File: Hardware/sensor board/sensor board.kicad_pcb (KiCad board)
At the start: 2 copper layers, 10 parts, among them J1 Raspberry_Pi_2_3, J2 Bar30, J3 LPS331AP, J4 Conn_01x04_Pin, J5 Conn_01x04_Pin, U1 MTi_3

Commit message: updated 3d models
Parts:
- J1: footprint Connector_PinHeader_2.54mm:PinHeader_2x20_P2.54mm_Vertical -> Connector_PinSocket_2.54mm:PinSocket_2x20_P2.54mm_Vertical
- J4, J5: footprint Connector_JST:JST_XH_B4B-XH-AM_1x04_P2.50mm_Vertical -> Connector_JST:JST_XH_B4B-XH-A_1x04_P2.50mm_Vertical

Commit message: layout for sensor board
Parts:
- moved R1 94.7 mm to (52.5, 58.8)
- moved R2 94.7 mm to (52.5, 61.8)
- moved FB1 92.5 mm to (63.5, 48.0), turned to -90 degrees
- moved C1 91.6 mm to (63.5, 53.1), turned to 90 degrees
- moved U1 89.9 mm to (50.5, 49.3), turned to 180 degrees
- moved J5 87.5 mm to (45.1, 66.6), turned to 90 degrees
- moved J2 69.8 mm to (32.3, 50.2), turned to -90 degrees
- moved J4 67.7 mm to (31.9, 66.7), turned to 90 degrees
- moved J3 67.1 mm to (30.8, 22.1)
- moved J1 65.9 mm to (22.1, 67.8)
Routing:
- net GND: track 0.00 -> 119.2 mm
- net +3.3V: track 0.00 -> 111.7 mm, vias 0 -> 1
- net /SCL: track 0.00 -> 75.9 mm, vias 0 -> 1
- net /SDA: track 0.00 -> 66.8 mm, vias 0 -> 1
- net Net-(U1-VDDA): track 0.00 -> 8.72 mm

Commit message: Update sensor board.kicad_pcb
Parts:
- moved J5 20.8 mm to (65.9, 66.6)
- moved R1 20.8 mm to (73.3, 58.8)
- moved R2 20.8 mm to (73.3, 61.8)
- moved U1 20.8 mm to (71.3, 49.3)
- moved FB1 20.1 mm to (80.9, 58.1)
- moved C1 14.9 mm to (77.6, 58.0), turned to -90 degrees
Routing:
- net +3.3V: track 111.7 -> 117.5 mm
- net Net-(U1-VDDA): track 8.72 -> 13.8 mm
- net GND: track 119.2 -> 115.8 mm
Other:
- board outline added: 65.5 x 55.9 mm

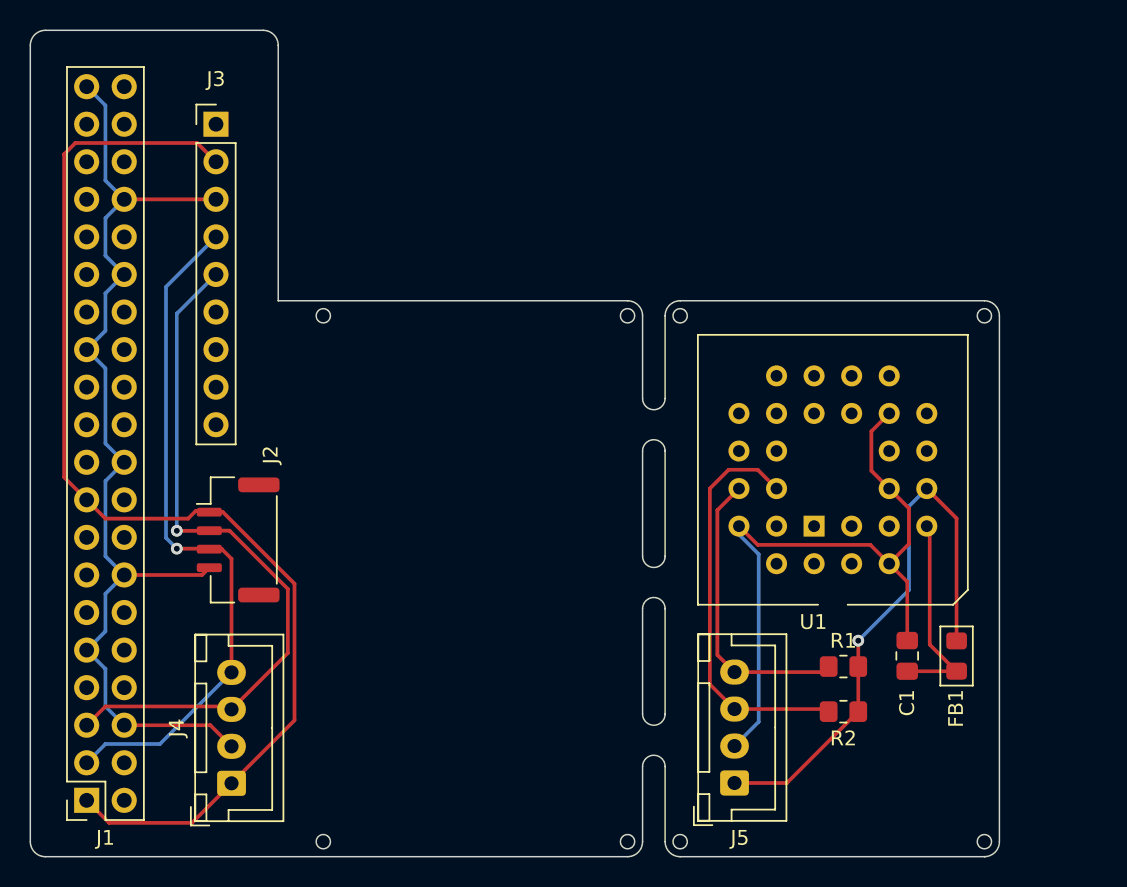
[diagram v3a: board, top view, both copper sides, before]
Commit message: updated outlines(needs ground plane)
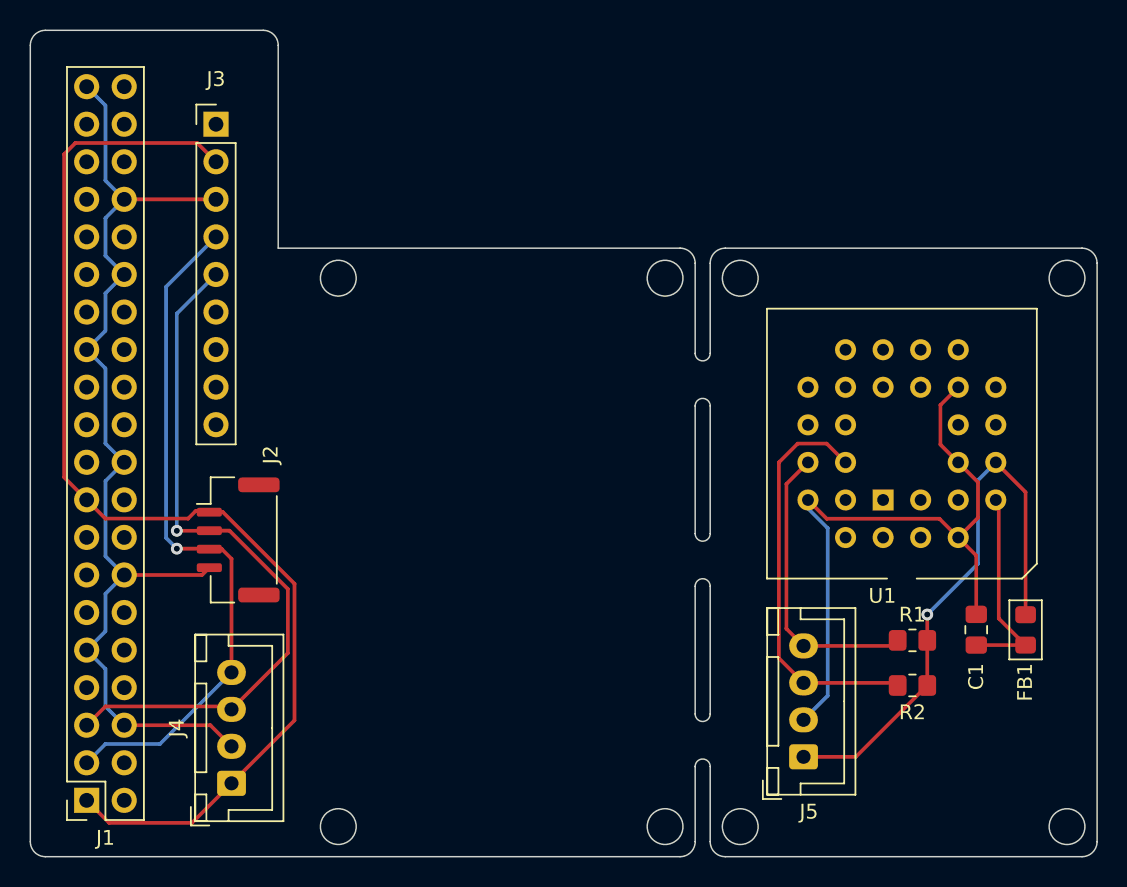
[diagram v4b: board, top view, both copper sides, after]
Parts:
- moved C1 4.99 mm to (82.3, 56.3)
- moved FB1 4.99 mm to (85.6, 56.3)
- moved R1 4.99 mm to (77.9, 57.0)
- moved R2 4.99 mm to (77.9, 60.0)
- moved U1 4.99 mm to (76.0, 47.5)
- moved J5 4.99 mm to (70.6, 64.9)
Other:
- board size 65.5 x 55.9 mm -> 72.1 x 55.9 mm

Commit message: added gnd plane
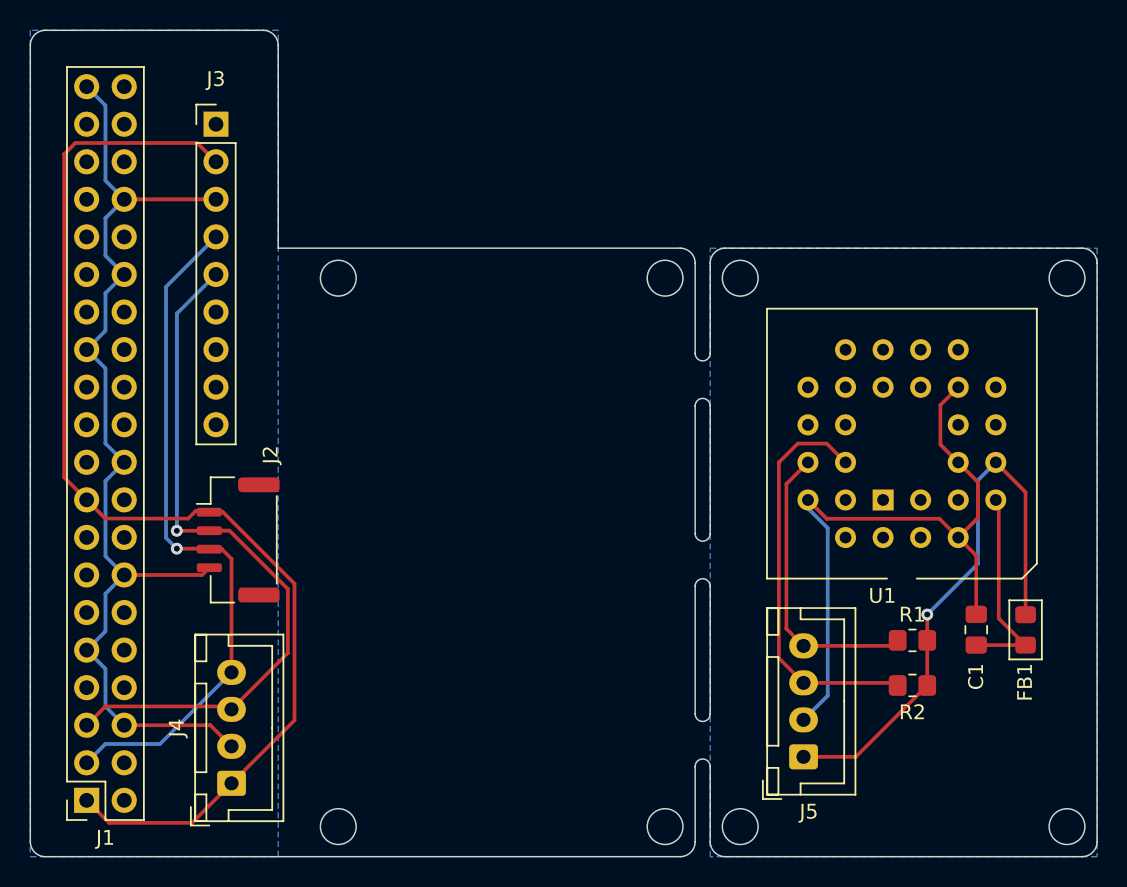
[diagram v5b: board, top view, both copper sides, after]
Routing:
- added copper zone on B.Cu, net GND
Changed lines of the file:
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@@
   (segment (start 28.194 34.908) (end 28.194 49.592156) (width 0.25) (layer "B.Cu") (net 7))
   (segment (start 30.844 32.258) (end 28.194 34.908) (width 0.25) (layer "B.Cu") (net 7))
+  (zone (net 1) (net_name "GND") (layer "B.Cu") (hatch edge 0.5)
+    (connect_pads yes (clearance 0.5))
+    (min_thickness 0.25) (filled_areas_thickness no)
+    (fill yes (thermal_gap 0.5) (thermal_bridge_width 0.5))
+    (polygon
+      (pts
+        (xy 18.288 15.748)
+        (xy 18.288 71.628)
+        (xy 35.052 71.628)
+        (xy 35.052 15.748)
+      )
+    )
+  )
+  (zone (net 1) (net_name "GND") (layer "B.Cu") (hatch edge 0.5)
+    (priority 1)
+    (connect_pads yes (clearance 0.5))
+    (min_thickness 0.25) (filled_areas_thickness no)
+    (fill yes (thermal_gap 0.5) (thermal_bridge_width 0.5))
+    (polygon
+      (pts
+        (xy 64.262 30.48)
+        (xy 90.424 30.48)
+        (xy 90.424 71.628)
+        (xy 64.262 71.628)
+      )
+    )
+  )
 )

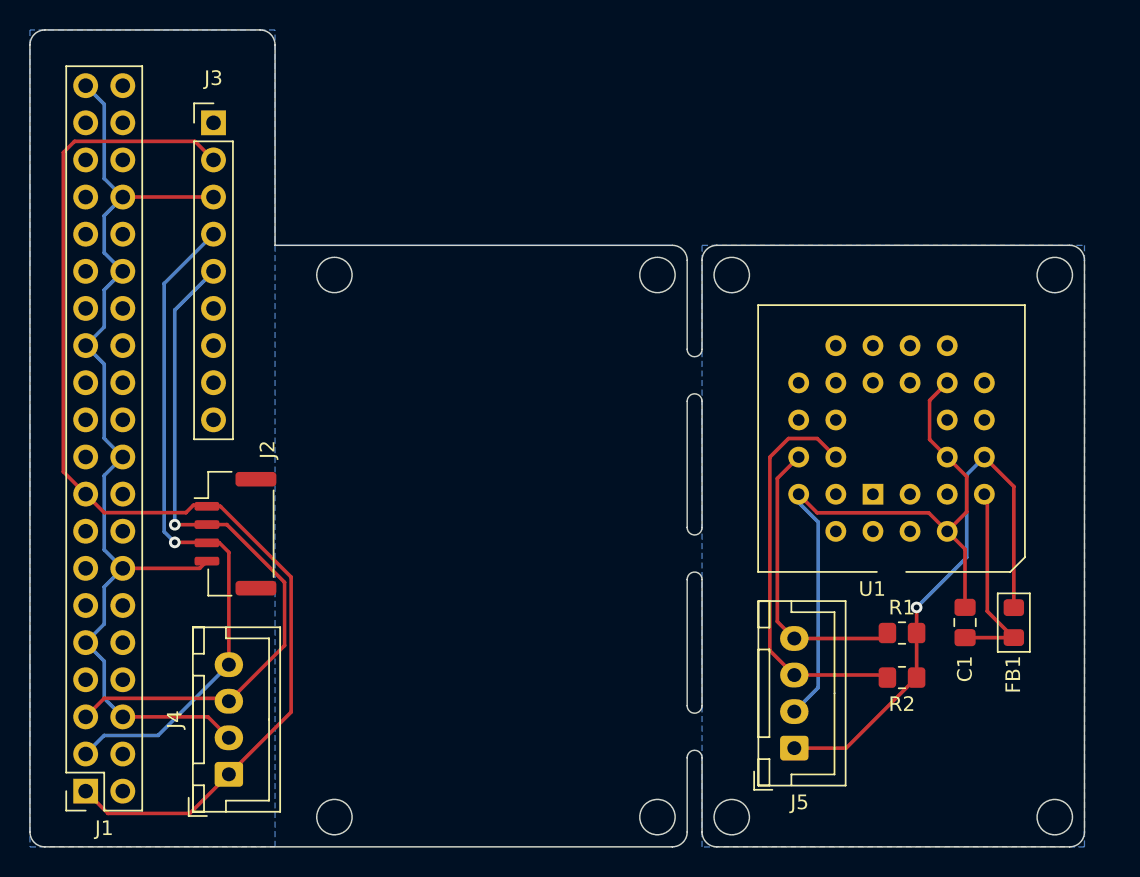
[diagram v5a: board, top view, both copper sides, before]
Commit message: modified traces + screw hole positions, added silkscreen
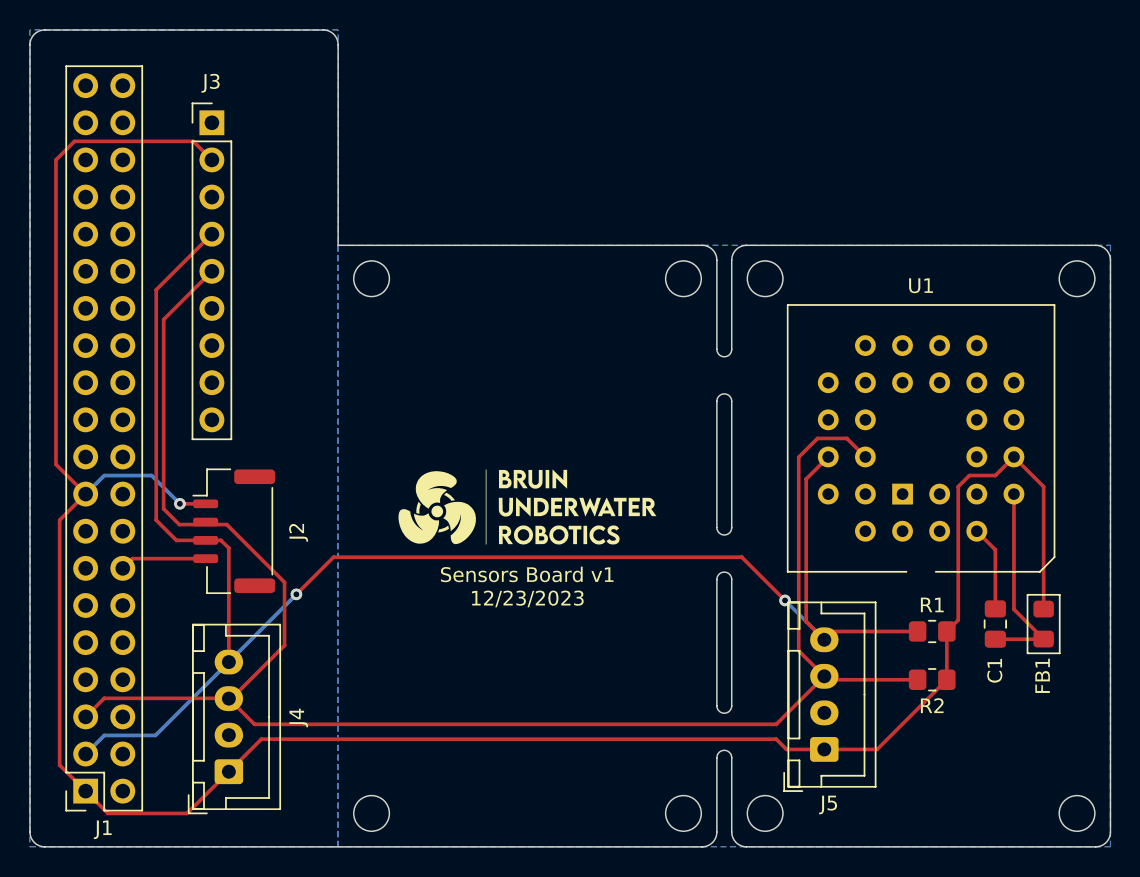
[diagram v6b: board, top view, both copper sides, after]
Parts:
- added G***: LOGO, LOGO, F.Cu at (52.3, 48.5)
- moved C1 2.08 mm to (84.3, 56.4)
- moved R2 2.07 mm to (80.0, 60.2)
- moved R1 2.07 mm to (80.0, 56.9)
- moved J5 2.05 mm to (72.6, 65.0)
- moved FB1 2.04 mm to (87.6, 56.4)
- moved U1 2.02 mm to (78.0, 47.5)
- moved J2 0.19 mm to (32.3, 50.0)
- moved J4 0.18 mm to (31.9, 66.5)
- moved J3 0.11 mm to (30.7, 22.1)
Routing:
- net GND: track 115.8 -> 11.8 mm
- net /SDA: track 66.8 -> 113.3 mm, vias 1 -> 2
- net +3.3V: track 117.5 -> 161.3 mm
- net /SCL: track 75.9 -> 119.3 mm, vias 1 -> 0
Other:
- board size 72.1 x 55.9 mm -> 73.9 x 55.9 mm
- board text added: "Sensors Board v1 12/23/2023"

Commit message: Update sensor board.kicad_pcb
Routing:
- net GND: track 11.8 -> 17.9 mm
- net +3.3V: track 161.3 -> 158.6 mm
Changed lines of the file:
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@@
   (gr_arc (start 66.294 37.595059) (mid 65.786 38.103059) (end 65.278 37.595059)
     (stroke (width 0.1) (type default)) (layer "Edge.Cuts"))
-  (gr_line (start 66.294 65.535059) (end 66.294 70.615059)
+  (gr_line (start 66.294 65.532) (end 66.294 70.612)
     (stroke (width 0.1) (type default)) (layer "Edge.Cuts"))
   (gr_arc (start 65.278 53.343059) (mid 65.786 52.835059) (end 66.294 53.343059)
@@
       (effects (font (size 1 1) (thickness 0.15)))
     )
-    (format (prefix "") (suffix "") (units 3) (units_format 1) (precision 4))
+    (format (prefix "") (suffix "") (units 1) (units_format 1) (precision 4))
     (style (thickness 0.15) (arrow_length 1.27) (text_position_mode 0) (extension_height 0.58642) (extension_offset 0.5) keep_text_aligned)
   )
@@
       (effects (font (size 1 1) (thickness 0.15)))
     )
-    (format (prefix "") (suffix "") (units 3) (units_format 1) (precision 4))
+    (format (prefix "") (suffix "") (units 1) (units_format 1) (precision 4))
     (style (thickness 0.15) (arrow_length 1.27) (text_position_mode 0) (extension_height 0.58642) (extension_offset 0.5) keep_text_aligned)
   )
@@
       (effects (font (size 1 1) (thickness 0.15)))
     )
-    (format (prefix "") (suffix "") (units 3) (units_format 1) (precision 4))
+    (format (prefix "") (suffix "") (units 1) (units_format 1) (precision 4))
     (style (thickness 0.15) (arrow_length 1.27) (text_position_mode 0) (extension_height 0.58642) (extension_offset 0.5) keep_text_aligned)
   )
@@
       (effects (font (size 1 1) (thickness 0.15)))
     )
-    (format (prefix "") (suffix "") (units 3) (units_format 1) (precision 4))
+    (format (prefix "") (suffix "") (units 1) (units_format 1) (precision 4))
     (style (thickness 0.15) (arrow_length 1.27) (text_position_mode 0) (extension_height 0.58642) (extension_offset 0.5) keep_text_aligned)
   )
@@
       (effects (font (size 1 1) (thickness 0.15)))
     )
-    (format (prefix "") (suffix "") (units 3) (units_format 1) (precision 4))
+    (format (prefix "") (suffix "") (units 1) (units_format 1) (precision 4))
     (style (thickness 0.15) (arrow_length 1.27) (text_position_mode 0) (extension_height 0.58642) (extension_offset 0.5) keep_text_aligned)
   )
@@
     (style (thickness 0.15) (arrow_length 1.27) (text_position_mode 0) (extension_height 0.58642) (extension_offset 0.5) keep_text_aligned)
   )
+  (dimension (type aligned) (layer "User.2")
+    (pts (xy 88.6968 32.766) (xy 91.1352 32.766))
+    (height 3.556)
+    (gr_text "96.0000 mils" (at 89.916 35.172) (layer "User.2")
+      (effects (font (size 1 1) (thickness 0.15)))
+    )
+    (format (prefix "") (suffix "") (units 1) (units_format 1) (precision 4))
+    (style (thickness 0.15) (arrow_length 1.27) (text_position_mode 0) (extension_height 0.58642) (extension_offset 0.5) keep_text_aligned)
+  )
   (segment (start 83.058 50.038) (end 84.328 51.308) (width 0.25) (layer "F.Cu") (net 1))
   (segment (start 25.303 51.913) (end 24.638 52.578) (width 0.25) (layer "F.Cu") (net 1))
+  (segment (start 81.788 48.768) (end 81.788 46.228) (width 0.25) (layer "F.Cu") (net 1))
+  (segment (start 83.058 50.038) (end 81.788 48.768) (width 0.25) (layer "F.Cu") (net 1))
+  (segment (start 81.788 46.228) (end 83.058 44.958) (width 0.25) (layer "F.Cu") (net 1))
   (segment (start 84.328 51.308) (end 84.328 55.3505) (width 0.25) (layer "F.Cu") (net 1))
   (segment (start 84.328 55.3505) (end 84.327869 55.3505) (width 0.25) (layer "F.Cu") (net 1))
@@
   (segment (start 20.066 45.466) (end 20.066 24.638) (width 0.25) (layer "F.Cu") (net 3))
   (segment (start 70.044 64.964) (end 72.627 64.964) (width 0.25) (layer "F.Cu") (net 3))
-  (segment (start 81.788 46.99) (end 82.55 46.228) (width 0.25) (layer "F.Cu") (net 3))
+  (segment (start 87.122 60.198) (end 88.9 58.42) (width 0.25) (layer "F.Cu") (net 3))
   (segment (start 87.63 55.363) (end 87.63 46.99) (width 0.25) (layer "F.Cu") (net 3))
+  (segment (start 88.9 58.42) (end 88.9 56.633) (width 0.25) (layer "F.Cu") (net 3))
   (segment (start 22.098 67.818) (end 23.622 69.342) (width 0.25) (layer "F.Cu") (net 3))
   (segment (start 29.464 23.368) (end 30.734 24.638) (width 0.25) (layer "F.Cu") (net 3))
-  (segment (start 81.01 56.896) (end 81.788 56.118) (width 0.25) (layer "F.Cu") (net 3))
   (segment (start 23.622 69.342) (end 29.04 69.342) (width 0.25) (layer "F.Cu") (net 3))
   (segment (start 69.342 64.262) (end 70.044 64.964) (width 0.25) (layer "F.Cu") (net 3))
@@
   (segment (start 76.244 64.964) (end 81.01 60.198) (width 0.25) (layer "F.Cu") (net 3))
   (segment (start 34.12 64.262) (end 69.342 64.262) (width 0.25) (layer "F.Cu") (net 3))
-  (segment (start 81.788 56.118) (end 81.788 46.99) (width 0.25) (layer "F.Cu") (net 3))
   (segment (start 20.32 49.276) (end 22.098 47.498) (width 0.25) (layer "F.Cu") (net 3))
-  (segment (start 84.328 46.228) (end 85.598 44.958) (width 0.25) (layer "F.Cu") (net 3))
+  (segment (start 88.9 56.633) (end 87.63 55.363) (width 0.25) (layer "F.Cu") (net 3))
   (segment (start 72.627 64.964) (end 76.244 64.964) (width 0.25) (layer "F.Cu") (net 3))
-  (segment (start 82.55 46.228) (end 84.328 46.228) (width 0.25) (layer "F.Cu") (net 3))
+  (segment (start 81.01 60.198) (end 87.122 60.198) (width 0.25) (layer "F.Cu") (net 3))
   (segment (start 87.63 46.99) (end 85.598 44.958) (width 0.25) (layer "F.Cu") (net 3))
   (via (at 28.545 48.163) (size 0.8) (drill 0.4) (layers "F.Cu" "B.Cu") (net 3))
